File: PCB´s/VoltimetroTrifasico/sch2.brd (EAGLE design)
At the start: 160 x 100 mm, 25 parts, among them IC1 LM324N

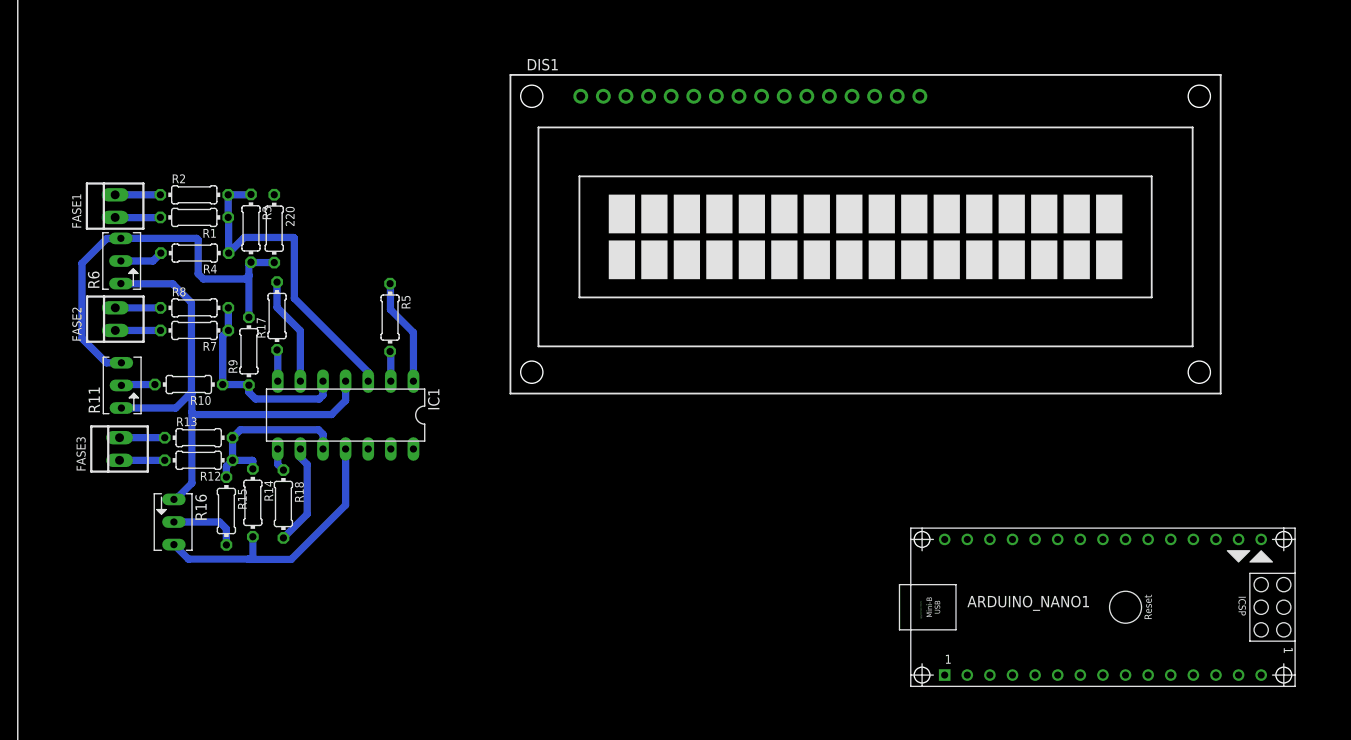
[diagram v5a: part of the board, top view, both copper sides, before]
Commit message: Rutas con Arduino y se agrego mol para fuente
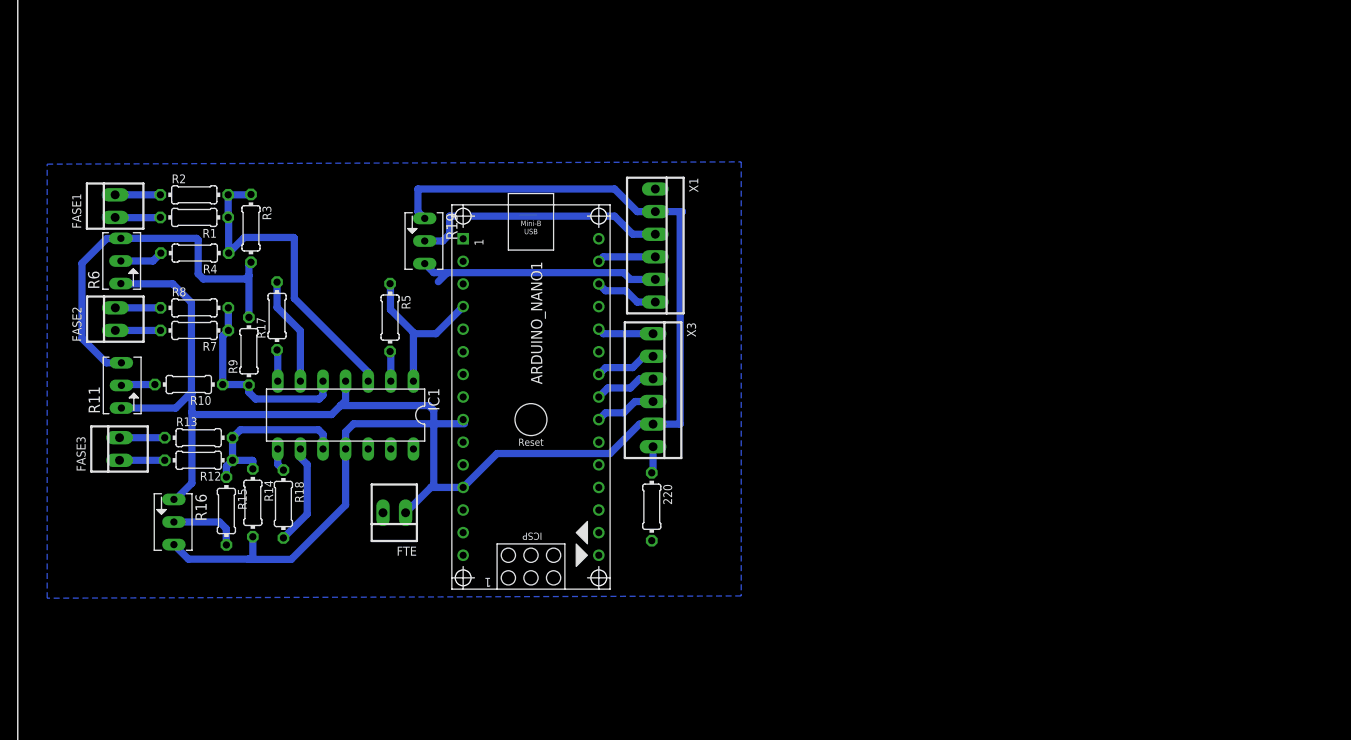
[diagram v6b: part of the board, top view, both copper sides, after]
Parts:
- removed DIS1: TUXGR_16X2_R2, display-lcd:TUXGR_16X2_R2
- added FTE: FTE, con-molex:22-23-2021
- added R19: (no value), pot:B64Y
- added X1: LCD1, con-molex:22-23-2061
- added X3: LCD2, con-molex:22-23-2061
- moved ARDUINO_NANO1 70.0 mm to (57.7, 37.6), turned to 270 degrees
- moved 220 52.7 mm to (71.2, 27.8)
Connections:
- removed net N$3: 220.1, DIS1.16
- new net RES: 220.1, X3.6
- net +5V: now also FTE.1, R19.E, X1.2, X3.5; no longer DIS1.15, DIS1.2
- net D4: now also X3.1; no longer DIS1.11
- net D5: now also X3.2; no longer DIS1.12
- net D6: now also X3.3; no longer DIS1.13
- net D7: now also X3.4; no longer DIS1.14
- net ENA: now also X1.6; no longer DIS1.6
- net GND: now also FTE.2, R19.A, X1.1, X1.5; no longer DIS1.1, DIS1.5
- net RS: now also X1.4; no longer DIS1.4
- net V0: now also R19.S, X1.3; no longer DIS1.3
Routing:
- net +5V: track 60.7 -> 173.5 mm
- net GND: track 79.0 -> 120.1 mm
- net V0: track 0.00 -> 29.1 mm
- net ENA: track 0.00 -> 7.19 mm
- net D6: track 0.00 -> 6.94 mm
- net D7: track 0.00 -> 6.94 mm
- net D5: track 0.00 -> 6.94 mm
- net AN0: track 12.0 -> 18.9 mm
- net RS: track 0.00 -> 6.56 mm
- net D4: track 0.00 -> 6.31 mm
- net RES: track 0.00 -> 2.99 mm
- added copper zone on layer 16, net GND

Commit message: ruteo terminado
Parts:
- moved R18 3.54 mm to (33.4, 28.6), turned to 0 degrees
- moved R17 2.41 mm to (31.1, 47.8), turned to 315 degrees
- moved R5 1.86 mm to (43.0, 47.6), turned to 180 degrees
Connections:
- net AN0: now also IC1.7, R17.1; no longer IC1.1, R5.1
- net AN1: now also IC1.1, R5.1; no longer IC1.7, R17.1
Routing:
- net AN2: track 2.63 -> 68.9 mm, vias 0 -> 2
- net GND: track 120.1 -> 75.8 mm
- net AN0: track 18.9 -> 35.0 mm, vias 0 -> 2
- net N$5: track 12.2 -> 4.03 mm
- net AN1: track 3.54 -> 9.97 mm
- net N$2: track 3.37 -> 6.81 mm
- net N$1: track 11.4 -> 9.87 mm
